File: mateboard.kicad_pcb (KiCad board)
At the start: 6 copper layers, 70 x 50 mm, 178 parts, among them IC1 OSD335x, IC2 SN74LVC2G241DCUR, IC3 NAND_4GB, IC4 WL1835MODGBMOCT, J1 IO1, J10 TEST_1P, J11 TEST_1P, J12 ANT2, J13 TEST_1P, J14 TEST_1P, J15 VDDS_PLL, J16 VDDS_DDR, J17 VDD_MPU, J18 VDD_CORE, J2 IO2, J3 GS2, J4 ANT2, J5 TEST_1P, J6 TEST_1P, J7 TEST_1P, J8 TEST_1P, J9 TEST_1P, Q1 BSS138, Q2 BSS138, U1 AP2112K-3.3TRG1, U10 TXS0108, U11 TXS0108, U2 AP2112K-1.8TRG1, U3 TL1963A-33DCQR, U4 24LC32AT-I, U5 TPS2065CDGN, U6 TPD4S012, U7 TPD4S012, U8 SN74LVC1G06DCK, U9 74LVC1G07DCK, X1 NZ2520SB-32.768KHZ-NSA3534C, Y1 24MHz, Y2 32.768kHz

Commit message: arranging signals
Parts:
- added J19: VDD_3V3AUX, Measurement_Points:Measurement_Point_Round-SMD-Pad_Small, B.Cu at (138.4, 125.2)
- IC4: footprint bbblue:BeagleBone_Blue-GHI-IC_MOC-100(TI) -> footprints:BeagleBone_Blue-GHI-IC_MOC-100(TI)
- moved J2 209.1 mm to (112.5, 154.7), turned to 90 degrees
- moved AE1 179.6 mm to (92.2, 142.4)
- moved C1 179.6 mm to (146.8, 122.3)
- moved C10 179.6 mm to (106.3, 113.0)
- moved C11 179.6 mm to (120.1, 152.8)
- moved C12 179.6 mm to (126.2, 156.6)
- moved C14 179.6 mm to (122.6, 132.1)
- moved C15 179.6 mm to (122.6, 134.3)
- moved C17 179.6 mm to (120.1, 140.7)
- moved C18 179.6 mm to (121.4, 142.7)
- moved C19 179.6 mm to (121.3, 145.7)
- moved C2 179.6 mm to (119.4, 122.4)
- moved C20 179.6 mm to (142.2, 122.8)
- moved C22 179.6 mm to (140.5, 118.5)
- moved C23 179.6 mm to (123.9, 113.7)
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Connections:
- IC1 pad Y11: VDD_3V3AUX -> Net-(IC1-PadY11)
- J1 pad 10: /VBAT_TEMP -> /LCD_DATA14
- J1 pad 11: USB_DC -> /VBAT_SENSE
- J1 pad 12: /GPIO1_28 -> /LCD_DATA13
- J1 pad 13: /USB0_DM -> /VBAT_TEMP
- J1 pad 14: /CLKOUT1 -> /LCD_DATA12
- J1 pad 15: /USB0_DP -> Net-(J1-Pad15)
- J1 pad 16: /CLKOUT2 -> /LCD_DATA11
- J1 pad 17: /USB0_ID -> Net-(J1-Pad17)
- J1 pad 18: GNDD -> /LCD_DATA10
- J1 pad 19: GNDD -> Net-(J1-Pad19)
- J1 pad 20: /SD_BOOT -> /LCD_DATA9
- J1 pad 21: /USB1_VBUS -> Net-(J1-Pad21)
- J1 pad 22: /SD.CD -> /LCD_DATA8
- J1 pad 23: /USB1_DM -> Net-(J1-Pad23)
- J1 pad 24: /SD.CLK -> /LCD_DATA7
- J1 pad 25: /USB1_DP -> Net-(J1-Pad25)
- J1 pad 26: /SD.CMD -> /LCD_DATA6
- J1 pad 27: /LCD_DATA15 -> Net-(J1-Pad27)
- J1 pad 28: /SD.D3 -> /LCD_DATA5
- J1 pad 29: /LCD_DATA14 -> Net-(J1-Pad29)
- J1 pad 30: /SD.D2 -> /LCD_DATA4
- J1 pad 31: /LCD_DATA13 -> Net-(J1-Pad31)
- J1 pad 32: /SD.D1 -> /LCD_DATA3
- J1 pad 33: /LCD_DATA12 -> Net-(J1-Pad33)
- J1 pad 34: /SD.D0 -> /LCD_DATA2
- J1 pad 35: /LCD_DATA11 -> Net-(J1-Pad35)
- J1 pad 36: GNDD -> /LCD_DATA1
- J1 pad 37: /LCD_DATA10 -> Net-(J1-Pad37)
- J1 pad 38: /USR0 -> /LCD_DATA0
- J1 pad 39: /LCD_DATA9 -> Net-(J1-Pad39)
- J1 pad 40: /USR1 -> /LCD_HSYNC
- J1 pad 41: /LCD_DATA8 -> Net-(J1-Pad41)
- J1 pad 42: /USR2 -> /LCD_VSYNC
- J1 pad 43: /LCD_DATA7 -> Net-(J1-Pad43)
- J1 pad 44: /USR3 -> /LCD_PCLK
- J1 pad 45: /LCD_DATA6 -> Net-(J1-Pad45)
- J1 pad 46: GNDD -> /LCD_DE
- J1 pad 47: /LCD_DATA5 -> Net-(J1-Pad47)
- J1 pad 48: /JTAG_EMU1 -> Net-(J1-Pad48)
- J1 pad 49: /LCD_DATA4 -> Net-(J1-Pad49)
- J1 pad 5: /VBAT -> GNDD
- J1 pad 50: /JTAG_EMU0 -> Net-(J1-Pad50)
- J1 pad 51: /LCD_DATA3 -> Net-(J1-Pad51)
- J1 pad 52: /JTAG_TDO -> Net-(J1-Pad52)
- J1 pad 53: /LCD_DATA2 -> Net-(J1-Pad53)
- J1 pad 54: /JTAG_TCK -> Net-(J1-Pad54)
- J1 pad 55: /LCD_DATA1 -> Net-(J1-Pad55)
- J1 pad 56: /JTAG_TDI -> Net-(J1-Pad56)
- J1 pad 57: /LCD_DATA0 -> Net-(J1-Pad57)
- J1 pad 58: /JTAG_TMS -> Net-(J1-Pad58)
- J1 pad 59: /LCD_HSYNC -> Net-(J1-Pad59)
- J1 pad 6: /PWR_BUT -> GNDD
- J1 pad 60: /JTAG_TRSTn -> Net-(J1-Pad60)
- J1 pad 61: /LCD_VSYNC -> Net-(J1-Pad61)
- J1 pad 62: /TIMER4 -> Net-(J1-Pad62)
- J1 pad 63: /LCD_PCLK -> Net-(J1-Pad63)
- J1 pad 64: /TIMER5 -> Net-(J1-Pad64)
- J1 pad 65: /LCD_DE -> Net-(J1-Pad65)
- J1 pad 66: /TIMER6 -> Net-(J1-Pad66)
- J1 pad 67: /SYS_RESETn -> Net-(J1-Pad67)
- J1 pad 68: /TIMER7 -> Net-(J1-Pad68)
- J1 pad 69: GNDD -> Net-(J1-Pad69)
- J1 pad 70: GNDD -> Net-(J1-Pad70)
- J1 pad 8: /VBAT_SENSE -> /LCD_DATA15
- J1 pad 9: GNDD -> /VBAT
- J2 pad 1: /I2C0_SCL -> Net-(J2-Pad1)
- J2 pad 10: GNDD -> Net-(J2-Pad10)
- J2 pad 11: GNDD -> Net-(J2-Pad11)
- J2 pad 12: /GPIO0_7 -> Net-(J2-Pad12)
- J2 pad 13: /I2C2_SCL -> Net-(J2-Pad13)
- J2 pad 14: /GPIO3_21 -> Net-(J2-Pad14)
- J2 pad 15: /I2C2_SDA -> Net-(J2-Pad15)
- J2 pad 16: /GPIO3_19 -> Net-(J2-Pad16)
- J2 pad 17: GNDD -> Net-(J2-Pad17)
- J2 pad 18: /GPIO1_27 -> Net-(J2-Pad18)
- J2 pad 19: GNDD -> Net-(J2-Pad19)
- J2 pad 2: /eHRPWM2B -> Net-(J2-Pad2)
- J2 pad 20: GNDA -> Net-(J2-Pad20)
- J2 pad 21: GNDD -> Net-(J2-Pad21)
- J2 pad 22: /AIN0 -> Net-(J2-Pad22)
- J2 pad 23: /UART0_RXD -> Net-(J2-Pad23)
- J2 pad 24: GNDA -> Net-(J2-Pad24)
- J2 pad 25: /UART0_TXD -> Net-(J2-Pad25)
- J2 pad 26: /AIN1 -> Net-(J2-Pad26)
- J2 pad 27: /UART1_RXD -> Net-(J2-Pad27)
- J2 pad 28: GNDA -> Net-(J2-Pad28)
- J2 pad 29: /UART1_TXD -> Net-(J2-Pad29)
- J2 pad 3: /I2C0_SDA -> Net-(J2-Pad3)
- J2 pad 30: /AIN2 -> Net-(J2-Pad30)
- J2 pad 31: /UART2_TXD -> Net-(J2-Pad31)
- J2 pad 32: GNDA -> Net-(J2-Pad32)
- J2 pad 33: /UART2_RXD -> Net-(J2-Pad33)
- J2 pad 34: /AIN3 -> Net-(J2-Pad34)
- J2 pad 35: /UART4_TXD -> Net-(J2-Pad35)
- J2 pad 36: GNDA -> Net-(J2-Pad36)
- J2 pad 37: /UART4_RXD -> Net-(J2-Pad37)
- J2 pad 38: /AIN4 -> Net-(J2-Pad38)
- J2 pad 39: /GPIO2_0 -> Net-(J2-Pad39)
- J2 pad 4: /eHRPWM2A -> Net-(J2-Pad4)
- J2 pad 40: GNDA -> Net-(J2-Pad40)
- J2 pad 41: /GPIO1_25 -> Net-(J2-Pad41)
- J2 pad 42: /AIN5 -> Net-(J2-Pad42)
- J2 pad 43: /GPIO1_29 -> Net-(J2-Pad43)
- J2 pad 44: GNDA -> Net-(J2-Pad44)
- J2 pad 45: /GPIO1_16 -> Net-(J2-Pad45)
- J2 pad 46: /AIN6 -> Net-(J2-Pad46)
- J2 pad 47: /GPIO1_15 -> Net-(J2-Pad47)
- J2 pad 48: GNDA -> Net-(J2-Pad48)
- J2 pad 49: /GPIO1_13 -> Net-(J2-Pad49)
- J2 pad 5: GNDD -> Net-(J2-Pad5)
- J2 pad 50: /AIN7 -> Net-(J2-Pad50)
- J2 pad 51: /GPIO1_14 -> Net-(J2-Pad51)
- J2 pad 52: GNDA -> Net-(J2-Pad52)
- J2 pad 53: /GPIO1_12 -> Net-(J2-Pad53)
- J2 pad 54: VDD_ADC -> Net-(J2-Pad54)
- J2 pad 55: /GPIO0_27 -> Net-(J2-Pad55)
- J2 pad 56: /GPIO1_17 -> Net-(J2-Pad56)
- J2 pad 57: /GPIO0_26 -> Net-(J2-Pad57)
- J2 pad 58: /SPI1_CLK -> Net-(J2-Pad58)
- J2 pad 59: /GPIO2_1 -> Net-(J2-Pad59)
- J2 pad 6: /eHRPWM1B -> Net-(J2-Pad6)
- J2 pad 60: /SPI1_D0 -> Net-(J2-Pad60)
- J2 pad 61: GNDD -> Net-(J2-Pad61)
- J2 pad 62: /SPI1_D1 -> Net-(J2-Pad62)
- J2 pad 63: GNDD -> Net-(J2-Pad63)
- J2 pad 64: /SPI1_CS0 -> Net-(J2-Pad64)
- J2 pad 65: VDD_3V3B -> Net-(J2-Pad65)
- J2 pad 66: SYS_5V -> Net-(J2-Pad66)
- J2 pad 67: VDD_3V3B -> Net-(J2-Pad67)
- J2 pad 68: SYS_5V -> Net-(J2-Pad68)
- J2 pad 69: GNDD -> Net-(J2-Pad69)
- J2 pad 7: /I2C1_SDA -> Net-(J2-Pad7)
- J2 pad 70: GNDD -> Net-(J2-Pad70)
- J2 pad 8: /eHRPWM1A -> Net-(J2-Pad8)
- J2 pad 9: /I2C1_SCL -> Net-(J2-Pad9)
- U11 pad 16: /CLKOUT2 -> /Wi-Fi BLE/CLKOUT2
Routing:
- net /PWR_BUT: track 61.0 -> 0.00 mm, vias 2 -> 0
- net /SYS_RESETn: track 37.8 -> 6.58 mm, vias 1 -> 0
- net /USB1_DP: track 37.9 -> 8.65 mm, vias 3 -> 2
- net /USB1_DM: track 35.3 -> 7.18 mm, vias 3 -> 2
- net /TIMER4: track 25.2 -> 0.90 mm
- net /LCD_DATA7: track 0.90 -> 21.5 mm, vias 1 -> 3
- net /LCD_DATA15: track 15.5 -> 35.8 mm, vias 2 -> 3
- net USB_DC: track 62.2 -> 43.6 mm, vias 5 -> 4
- net /LCD_DATA6: track 0.90 -> 18.0 mm, vias 1 -> 3
- net /USB1_VBUS: track 15.2 -> 0.00 mm, vias 1 -> 0
- net /LCD_DATA0: track 5.27 -> 19.4 mm, vias 0 -> 2
- net /LCD_DATA5: track 5.00 -> 18.0 mm, vias 0 -> 2
- net /LCD_HSYNC: track 2.75 -> 14.7 mm, vias 2 -> 1
- net /LCD_DATA8: track 2.40 -> 13.7 mm, vias 0 -> 1
- net /SD_BOOT: track 13.6 -> 2.65 mm
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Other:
- net class Default: clearance 0.15 -> 0.1
- rule trace_clearance: 0.15 -> 0.1

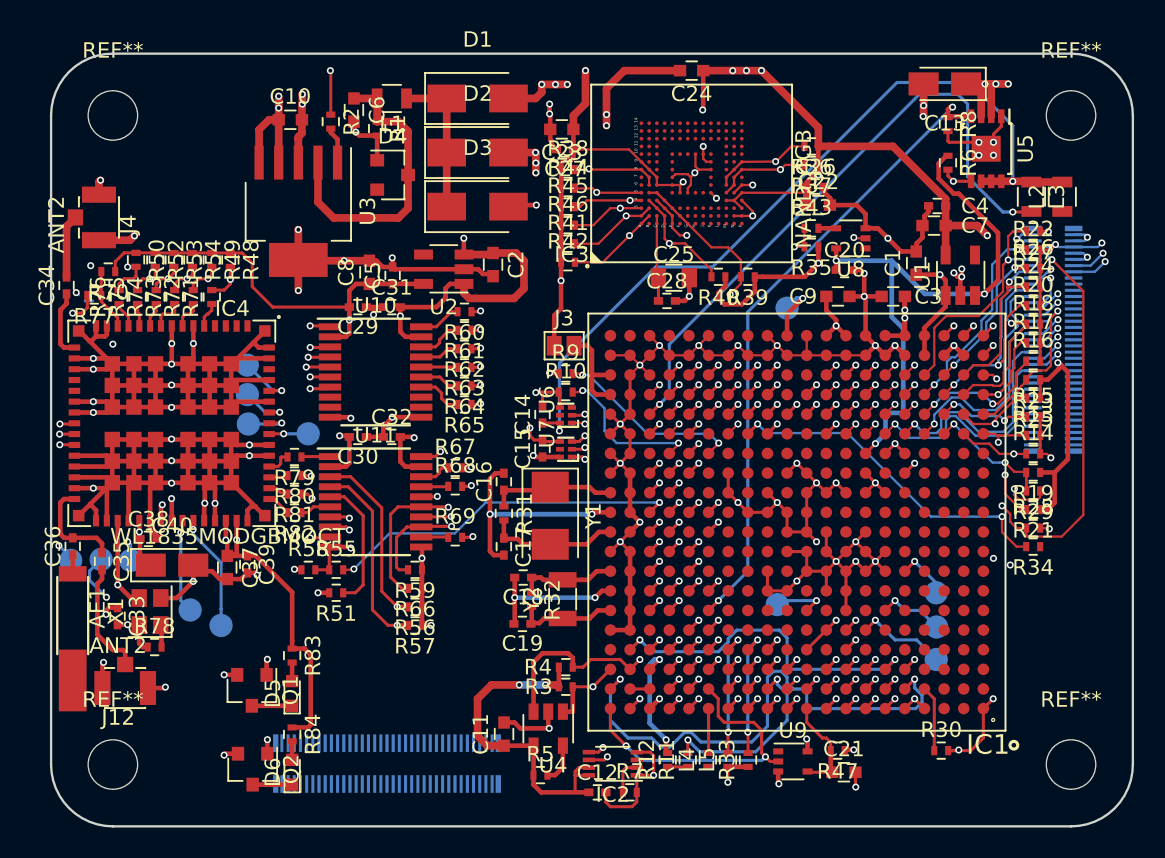
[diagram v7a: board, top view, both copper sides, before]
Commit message: j1 io routing done
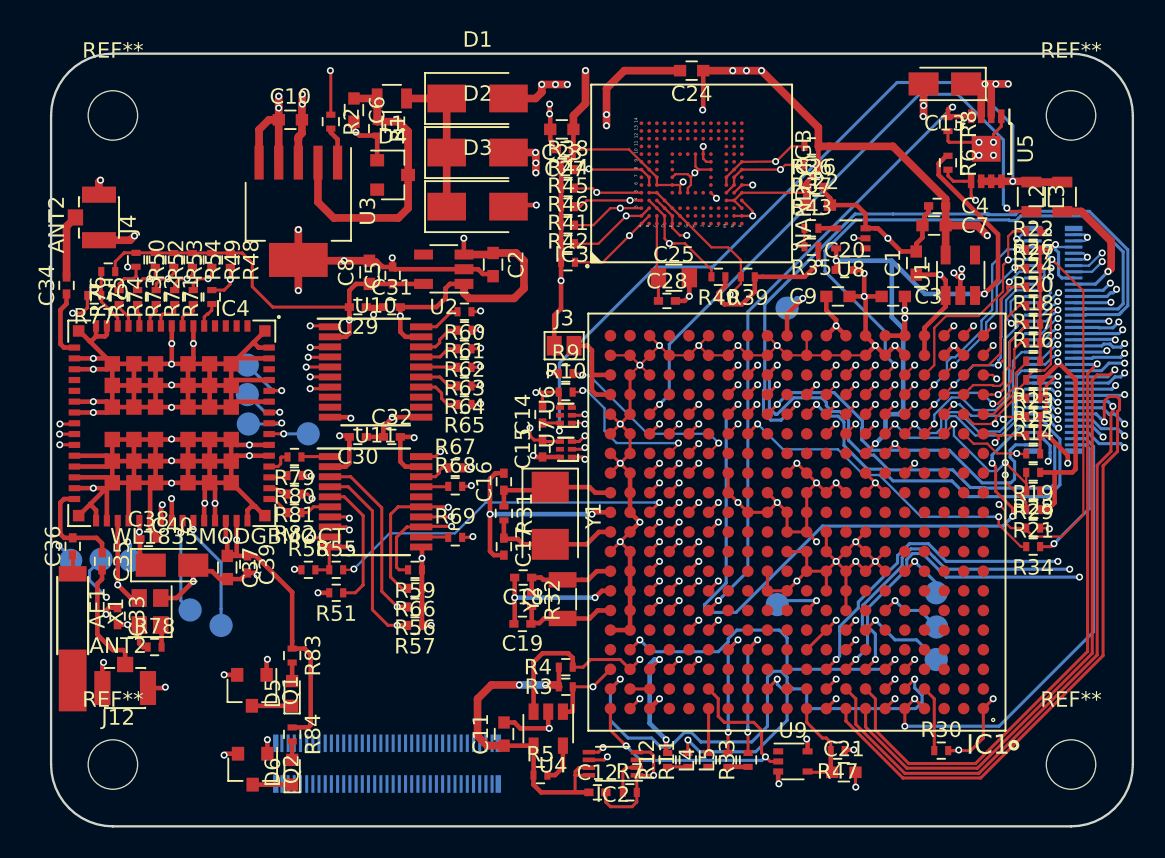
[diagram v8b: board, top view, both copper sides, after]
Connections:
- J1 pad 15: Net-(J1-Pad15) -> GNDD
- J1 pad 17: Net-(J1-Pad17) -> /USB1_VBUS
- J1 pad 19: Net-(J1-Pad19) -> /USB1_DM
- J1 pad 21: Net-(J1-Pad21) -> /USB1_DP
- J1 pad 23: Net-(J1-Pad23) -> GNDD
- J1 pad 25: Net-(J1-Pad25) -> /GPIO1_29
- J1 pad 27: Net-(J1-Pad27) -> /GPIO0_26
- J1 pad 29: Net-(J1-Pad29) -> /GPIO1_14
- J1 pad 31: Net-(J1-Pad31) -> /GPIO1_15
- J1 pad 33: Net-(J1-Pad33) -> /GPIO2_0
- J1 pad 35: Net-(J1-Pad35) -> /AIN0
- J1 pad 37: Net-(J1-Pad37) -> GNDA
- J1 pad 39: Net-(J1-Pad39) -> /AIN1
- J1 pad 41: Net-(J1-Pad41) -> GNDA
- J1 pad 43: Net-(J1-Pad43) -> /AIN2
- J1 pad 45: Net-(J1-Pad45) -> GNDA
- J1 pad 47: Net-(J1-Pad47) -> /AIN3
- J1 pad 48: Net-(J1-Pad48) -> GNDD
- J1 pad 49: Net-(J1-Pad49) -> GNDA
- J1 pad 50: Net-(J1-Pad50) -> /TIMER6
- J1 pad 51: Net-(J1-Pad51) -> /AIN4
- J1 pad 52: Net-(J1-Pad52) -> /TIMER5
- J1 pad 53: Net-(J1-Pad53) -> GNDA
- J1 pad 54: Net-(J1-Pad54) -> /TIMER7
- J1 pad 55: Net-(J1-Pad55) -> /AIN5
- J1 pad 56: Net-(J1-Pad56) -> /TIMER4
- J1 pad 57: Net-(J1-Pad57) -> GNDA
- J1 pad 58: Net-(J1-Pad58) -> /eHRPWM2A
- J1 pad 59: Net-(J1-Pad59) -> /AIN6
- J1 pad 60: Net-(J1-Pad60) -> /eHRPWM1A
- J1 pad 61: Net-(J1-Pad61) -> GNDA
- J1 pad 62: Net-(J1-Pad62) -> /eHRPWM2B
- J1 pad 63: Net-(J1-Pad63) -> /AIN7
- J1 pad 64: Net-(J1-Pad64) -> /eHRPWM1B
- J1 pad 65: Net-(J1-Pad65) -> GNDA
- J1 pad 66: Net-(J1-Pad66) -> /GPIO2_1
- J1 pad 67: Net-(J1-Pad67) -> VDD_ADC
- J1 pad 68: Net-(J1-Pad68) -> /GPIO0_27
- J1 pad 69: Net-(J1-Pad69) -> /GPIO1_16
- J1 pad 70: Net-(J1-Pad70) -> /GPIO1_12
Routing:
- net /GPIO2_0: track 0.90 -> 77.7 mm, vias 1 -> 2
- net /GPIO1_15: track 0.90 -> 74.0 mm, vias 1 -> 2
- net /GPIO1_14: track 0.90 -> 69.9 mm, vias 1 -> 2
- net /USB1_DP: track 8.65 -> 62.7 mm, vias 2 -> 3
- net /USB1_DM: track 7.18 -> 58.5 mm, vias 2 -> 3
- net /eHRPWM1B: track 0.90 -> 45.5 mm, vias 1 -> 3
- net /GPIO0_26: track 0.90 -> 45.5 mm
- net /AIN6: track 0.90 -> 44.0 mm
- net /AIN3: track 0.90 -> 42.3 mm
- net /AIN5: track 0.90 -> 41.8 mm
- net /AIN2: track 0.90 -> 41.0 mm
- net /AIN1: track 0.90 -> 38.6 mm, vias 1 -> 3
- net /GPIO1_29: track 0.90 -> 38.1 mm
- net /AIN4: track 0.90 -> 36.6 mm, vias 1 -> 3
- net /AIN7: track 0.90 -> 36.2 mm, vias 1 -> 3
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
